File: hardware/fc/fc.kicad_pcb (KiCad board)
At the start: 4 copper layers, 42 x 41 mm, 95 parts, among them J1 USB-C, J10 GPIO, J11 BUZZER, J2 ESC, J3 ELRS, J4 I2C, J5 GPS, J6 VTX, J7 CAM, J8 SWD, J9 UART, Q1 Si2319CDS, Q2 2N7002, U1 STM32F405RGT6, U2 ICM-42688-P, U3 W25Q128JVSIQ, U4 LMR33630BDDA, U5 AMS1117-3.3, U6 USBLC6-2SC6, Y1 8MHz

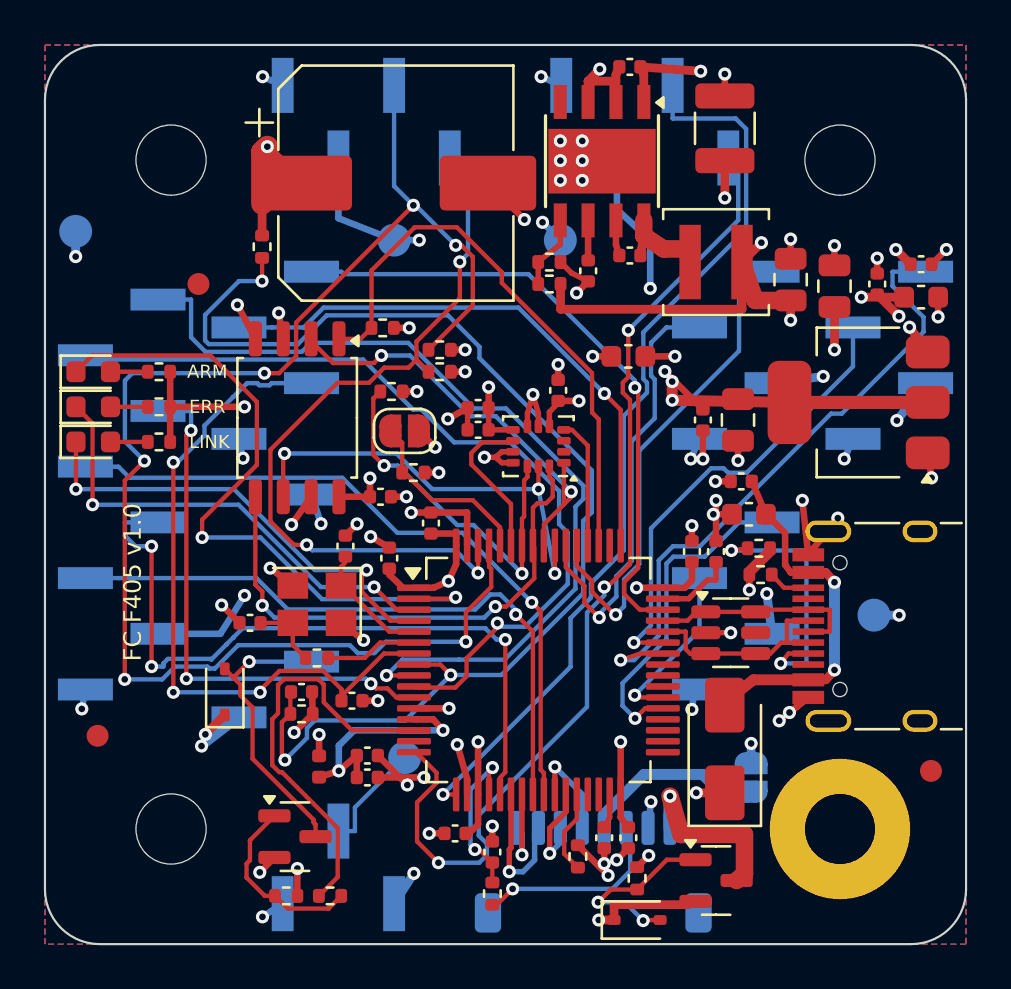
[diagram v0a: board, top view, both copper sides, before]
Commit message: FC: JST-SH-Buchsen unten, beidseitige JLCPCB-Bestückung
- Steckverbinder J3–J11 statt SMD-Stiftleisten jetzt JST-SH 1,0 mm
  (seitlich steckbar) wie J2; Randbuchsen an Nord-, West-, Ost- und
  Südkante, SWD und Piepser innen
- Versorgungspins der Buchsen per Handverdrahtung an die Flächen,
  M3/M4 fest vorverlegt; komplett neu geroutet (DRC 0/0, ERC 0 Fehler,
  Platine = Schaltplan 319 Pads)
- Fertigungsdaten für Standard-PCBA beider Seiten: BOM/CPL mit
  Unterseite (Megastar ZX-SH1.0, LCSC), Drehlagen aus Pad-Vergleich
  mit den JLC-Footprints (SOT-23 jetzt +180°, HSOP-8 +270° angenommen)
- README: Buchsenbelegung, Bestellablauf, Edge Rails, Prüfpunkte
- 3D-Ansichten und Lagenbilder erneuert

Co-Authored-By: Claude Opus 5.5 <noreply@anthropic.com>
Claude-Session: https://claude.ai/code/session_01JZYB7PZbCVuDQ6ovPGKpbm
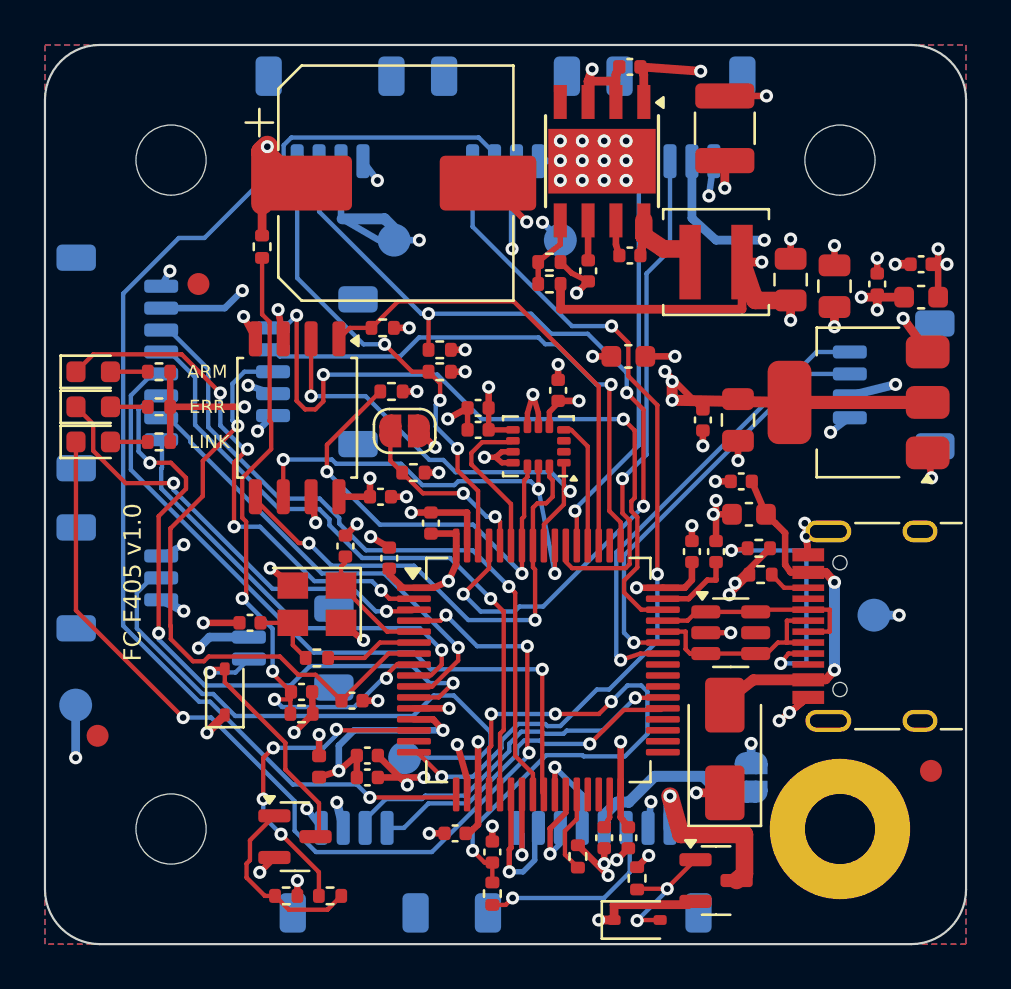
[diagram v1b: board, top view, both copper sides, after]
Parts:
- J10: footprint Connector_PinHeader_2.54mm:PinHeader_1x08_P2.54mm_Vertical_SMD_Pin1Left -> Connector_JST:JST_SH_SM08B-SRSS-TB_1x08-1MP_P1.00mm_Horizontal
- J11: footprint Connector_PinHeader_2.54mm:PinHeader_1x02_P2.54mm_Vertical_SMD_Pin1Left -> Connector_JST:JST_SH_SM02B-SRSS-TB_1x02-1MP_P1.00mm_Horizontal
- J3, J4, J5, J6, J9: footprint Connector_PinHeader_2.54mm:PinHeader_1x04_P2.54mm_Vertical_SMD_Pin1Left -> Connector_JST:JST_SH_SM04B-SRSS-TB_1x04-1MP_P1.00mm_Horizontal
- J7: footprint Connector_PinHeader_2.54mm:PinHeader_1x03_P2.54mm_Vertical_SMD_Pin1Left -> Connector_JST:JST_SH_SM03B-SRSS-TB_1x03-1MP_P1.00mm_Horizontal
- J8: footprint Connector_PinHeader_2.54mm:PinHeader_1x05_P2.54mm_Vertical_SMD_Pin1Left -> Connector_JST:JST_SH_SM05B-SRSS-TB_1x05-1MP_P1.00mm_Horizontal
- moved TP3 21.6 mm to (80.4, 109.6)
- moved J6 21.2 mm to (93.1, 117.2)
- moved J7 16.6 mm to (82.3, 103.8)
- moved J5 11.1 mm to (108.0, 82.8), turned to 0 degrees
- moved J9 6.35 mm to (100.0, 82.8), turned to 0 degrees
- moved J10 6.00 mm to (82.3, 94.0), turned to 90 degrees
- moved J11 2.05 mm to (90.3, 107.0), turned to -90 degrees
- moved J8 1.97 mm to (91.4, 94.4), turned to -90 degrees
- moved J4 1.66 mm to (92.0, 82.8), turned to 0 degrees
- moved J3 1.36 mm to (117.7, 95.0), turned to -90 degrees
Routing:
- net I2C_SCL: track 67.9 -> 40.6 mm, vias 6 -> 4
- net LED_LINK: track 20.9 -> 46.4 mm, vias 2 -> 4
- net VBAT_SENSE: track 54.9 -> 30.7 mm, vias 3 -> 4
- net GPIO1: track 40.6 -> 19.4 mm
- net CAM_VIDEO: track 5.04 -> 26.2 mm
- net CURR_SENSE: track 7.48 -> 26.3 mm, vias 2 -> 4
- net GPIO2: track 37.9 -> 20.7 mm
- net I2C_SDA: track 34.6 -> 22.1 mm
- net DBG_RX: track 41.9 -> 54.0 mm
- net VTX_RX: track 7.89 -> 16.1 mm
- net ELRS_TX: track 28.9 -> 21.4 mm
- net LED_ARM: track 31.3 -> 24.2 mm, vias 2 -> 4
- net GPIO3: track 24.5 -> 30.4 mm
- net FLASH_CS: track 26.2 -> 21.4 mm
- net DBG_TX: track 45.3 -> 40.7 mm
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
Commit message: FC: ELRS/GPS/I²C oben, Prüfbefunde behoben, 39 Teilenummern
- ELRS, I²C und GPS als JST-SH-Buchsen oben an der Westkante (im
  verschraubten Stack steckbar); LEDs östlich des Gyros, Fiducials
  versetzt; SWD und Piepser unten an die frei gewordenen Randplätze
- Prüfbefunde: C22 mit Masse direkt an PGND des LMR33630, Akku-Pfad
  0,8 mm mit je zwei Vias, VBAT-Streifen auf Lage 3 >= 2,5 mm, C7 direkt
  an VDDA, D1 weiter von der Kante, JP2 weg von der Massebohrung, UART-
  Buchse weg von den Wärmevias, Bestückungsdruck >= 1,0 mm / 0,16 mm
- Teilenummern 43 -> 39 (100 nF alle 50 V, 10 µF/25 V, 1 k, 5,1 k),
  Akkuteiler 100k/10k, Piepser-FET AO3400A
- route: Stichleitungen über ein Pad hinaus werden mit entfernt
- Außenkontur für den Rahmen (scripts/kontur.py, docs/fc_aussenkontur.txt)
- J2 (ESC) passt noch nicht zum UAngel-ESC und wird nach der Messung
  des Nutzers umgebaut – vorher nicht bestellen

DRC 0/0, ERC 0 Fehler, Platine = Schaltplan (319 Pads)

Co-Authored-By: Claude Opus 5.5 <noreply@anthropic.com>
Claude-Session: https://claude.ai/code/session_01JZYB7PZbCVuDQ6ovPGKpbm
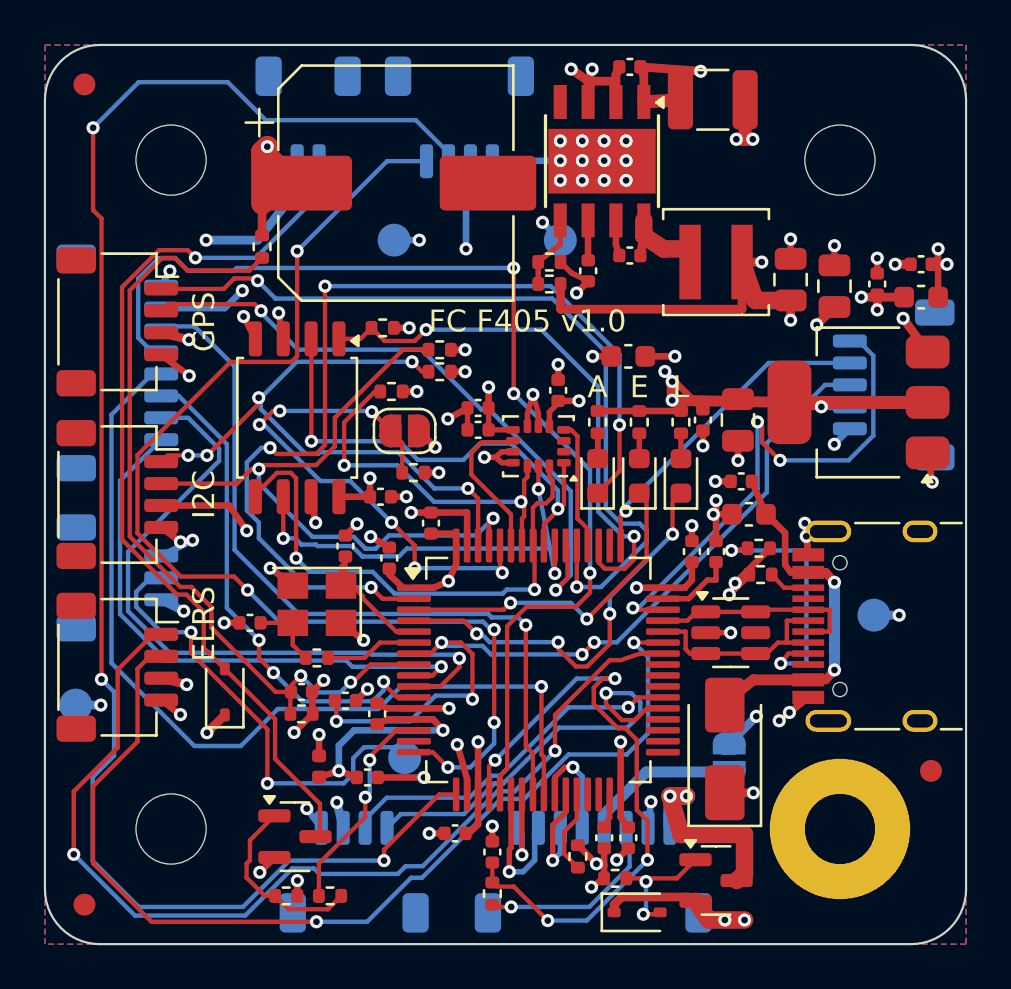
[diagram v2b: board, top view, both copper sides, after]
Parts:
- C29, C33: value 10uF -> 10uF/25V
- C6: value 4.7uF -> 10uF/25V
- J3, J4, J5: moved to F.Cu
- Q2: value 2N7002 -> AO3400A
- R17: value 100R -> 1k
- R19, R20: value 4.7k -> 5.1k
- R4: value 10k -> 100k
- R5: value 1k -> 10k
- moved J3 37.7 mm to (82.3, 107.9)
- moved J5 27.3 mm to (82.3, 92.1), turned to -90 degrees
- moved D5 26.8 mm to (108.0, 99.2), turned to 90 degrees
- moved J8 26.3 mm to (117.7, 95.0)
- moved D4 25.1 mm to (106.1, 99.2), turned to 90 degrees
- moved J11 24.2 mm to (91.0, 82.8), turned to 0 degrees
- moved R16 23.8 mm to (108.0, 96.7), turned to -90 degrees
- moved D3 23.5 mm to (104.2, 99.2), turned to 90 degrees
- moved R15 21.9 mm to (106.1, 96.7), turned to -90 degrees
- moved R14 20.1 mm to (104.2, 96.7), turned to -90 degrees
- moved J4 19.7 mm to (82.3, 100.0), turned to -90 degrees
- moved FID3 10.5 mm to (80.8, 81.3)
- moved FID1 7.72 mm to (80.8, 118.7)
- moved J9 2.10 mm to (97.9, 82.8)
- moved C7 1.95 mm to (94.2, 110.0), turned to 90 degrees
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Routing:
- net BUZ_N: track 12.1 -> 41.4 mm
- net LED_LINK: track 46.4 -> 18.1 mm
- net ELRS_RX: track 19.2 -> 46.2 mm, vias 1 -> 2
- net ELRS_TX: track 21.4 -> 45.6 mm, vias 1 -> 2
- net LED_ARM: track 24.2 -> 44.7 mm
- net GPIO5: track 30.0 -> 49.9 mm, vias 1 -> 3
- net GPS_TX: track 18.9 -> 37.7 mm, vias 1 -> 2
- net DBG_RX: track 54.0 -> 72.5 mm, vias 1 -> 3
- net BOOT0: track 8.60 -> 24.5 mm, vias 2 -> 6
- net DBG_TX: track 40.7 -> 52.8 mm, vias 3 -> 5
- net I2C_SCL: track 40.6 -> 29.9 mm, vias 4 -> 2
- net GPIO2: track 20.7 -> 31.2 mm
- net SWCLK: track 24.4 -> 14.8 mm
- net NRST: track 28.4 -> 37.3 mm, vias 1 -> 5
- net SWDIO: track 32.6 -> 23.9 mm
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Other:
- board text added: "A"
- board text added: "E"
- board text added: "L"
- board text removed: "ARM"
- board text removed: "ERR"
- board text removed: "LINK"

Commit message: FC: J2 auf B-Cube 4in1, getrennte 4,5-V-Schiene, C21 47 uF, Pfeil VORNE
- J2 nach Messung am B-Cube 4in1: 1 GND, 2 VBAT, 3-6 M1-M4, 7 Strom,
  8 NC (unbeschaltet), fuer 1:1-Kabel. JP2 und ESC_5V entfernt.
  Motorpins am Prozessor unveraendert (wie Sensors/motor.c).
- +4V5 wie bei Matek: VBUS -> D2 und +5V -> D7 (SS14, Unterseite) auf
  AMS1117, ELRS und GPS. VTX, Kamera und Piepser laufen an USB nicht mit.
- C21 470 uF -> 47 uF/35 V 6,3x5,4 (C48970990), Einschaltstrom.
- Nordkante = vorn: Pfeile und VORNE im Bestueckungsdruck.
- README: Firmware-Hinweise (NOVBUSSENS, DMA-Konflikt DShot/GPS-TX/
  Debug-RX, Gyro CW270 inkl. Betaflight ab 2025.12, ADC-Pins),
  J2-Lage von oben, Pruefanleitung vor dem ersten Akku.
- Neu geroutet, Aussen-GND Mindestbreite 0,25 mm; DRC 0, ERC 0 Fehler,
  Fertigungsdaten (74 oben, 8 unten, 39 Teilenummern) und Doku neu.

Co-Authored-By: Claude Opus 5.5 <noreply@anthropic.com>
Claude-Session: https://claude.ai/code/session_01JZYB7PZbCVuDQ6ovPGKpbm
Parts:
- removed JP2: ESC_5V, Jumper:SolderJumper-2_P1.3mm_Open_RoundedPad1.0x1.5mm
- added D7: SS14, Diode_SMD:D_SMA, B.Cu at (110.0, 110.4)
- C21: value 470uF/35V -> 47uF/35V; footprint Capacitor_SMD:CP_Elec_10x10.5 -> Capacitor_SMD:CP_Elec_6.3x5.4
- moved C21 2.00 mm to (93.0, 85.8)
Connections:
- C29 pad 1: +5V -> +4V5
- C30 pad 1: +5V -> +4V5
- D2 pad 1: +5V -> +4V5
- J2 pad 1: VBAT_IN -> GND
- J2 pad 2: GND -> VBAT_IN
- J2 pad 3: CURR_IN -> M1
- J2 pad 4: ESC_5V -> M2
- J2 pad 5: M1 -> M3
- J2 pad 6: M2 -> M4
- J2 pad 7: M3 -> CURR_IN
- J2 pad 8: M4 -> (no net)
- J3 pad 3: +5V -> +4V5
- J5 pad 3: +5V -> +4V5
- U5 pad 3: +5V -> +4V5
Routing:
- net +4V5: track 0.00 -> 86.8 mm, vias 0 -> 6
- net GPIO6: track 34.9 -> 71.2 mm
- net GPIO3: track 22.3 -> 49.4 mm, vias 3 -> 5
- net LED_ARM: track 44.7 -> 19.4 mm, vias 4 -> 2
- net ELRS_TX: track 45.6 -> 25.7 mm
- net ELRS_RX: track 46.2 -> 26.6 mm
- net BOOT0: track 24.5 -> 8.65 mm, vias 6 -> 0
- net DBG_RX: track 72.5 -> 58.2 mm
- net GPIO4: track 41.2 -> 30.6 mm
- net I2C_SCL: track 29.9 -> 38.9 mm, vias 2 -> 3
- net GPIO2: track 31.2 -> 22.9 mm
- net +5V: track 38.7 -> 30.7 mm, vias 16 -> 10
- net BUZ_N: track 41.4 -> 49.0 mm
- net GYRO_CS: track 16.5 -> 23.6 mm, vias 2 -> 4
- net ESC_5V: track 6.50 -> 0.00 mm
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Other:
- board text added: "VORNE"
- board text removed: "5V ESC"

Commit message: FC: Pruefbefunde Layout/Fertigung/README behoben
- +4V5 Diodenknoten -> AMS1117 unter der USB-C-Buchse nur noch auf B.Cu
  (vorher F.Cu direkt unter dem Blechgehaeuse), als Handverdrahtung;
  TP2 1 mm nach Osten.
- D1 um 180 Grad gedreht: Q1_G ohne Vias, der VBAT-Suedstreifen auf
  Lage 3 ist nicht mehr auf 0,7 mm eingeschnuert (jetzt 2,2 mm).
- GND-Anschluss J2 Pin 1 auf 0,5 mm, doppelte/Null-Bahnstuecke entfernt.
- BOM-Kommentar = Beschreibung des bestellten Teils statt Wert der
  ersten Referenz.
- README: gemessene VBAT-Breiten, Lage der Testpunkte, mkdir build,
  3D-Render-Befehl, Elko-Drehlage, LED-Ersatz, SPI-Laengen, Kennzahlen.
- DRC 0 (KiCad 7 und 9), 319 Pads ohne Abweichung; Fertigungsdaten,
  Doku und 3D-Ansichten neu.

Co-Authored-By: Claude Opus 5.5 <noreply@anthropic.com>
Claude-Session: https://claude.ai/code/session_01JZYB7PZbCVuDQ6ovPGKpbm
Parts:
- moved TP2 1.00 mm to (117.8, 105.5)
- turned D1 to 180 degrees
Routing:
- net VBAT: track 21.2 -> 19.5 mm
- net Q1_G: track 5.57 -> 4.99 mm, vias 2 -> 0
- net +4V5: track 86.8 -> 86.5 mm, vias 6 -> 7
